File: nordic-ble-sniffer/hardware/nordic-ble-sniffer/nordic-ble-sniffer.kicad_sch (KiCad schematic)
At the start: 23 parts, among them J2 USB2UART, U1 nRF52833_QDxx, U2 USBLC6-2P6, Y1 32MHz

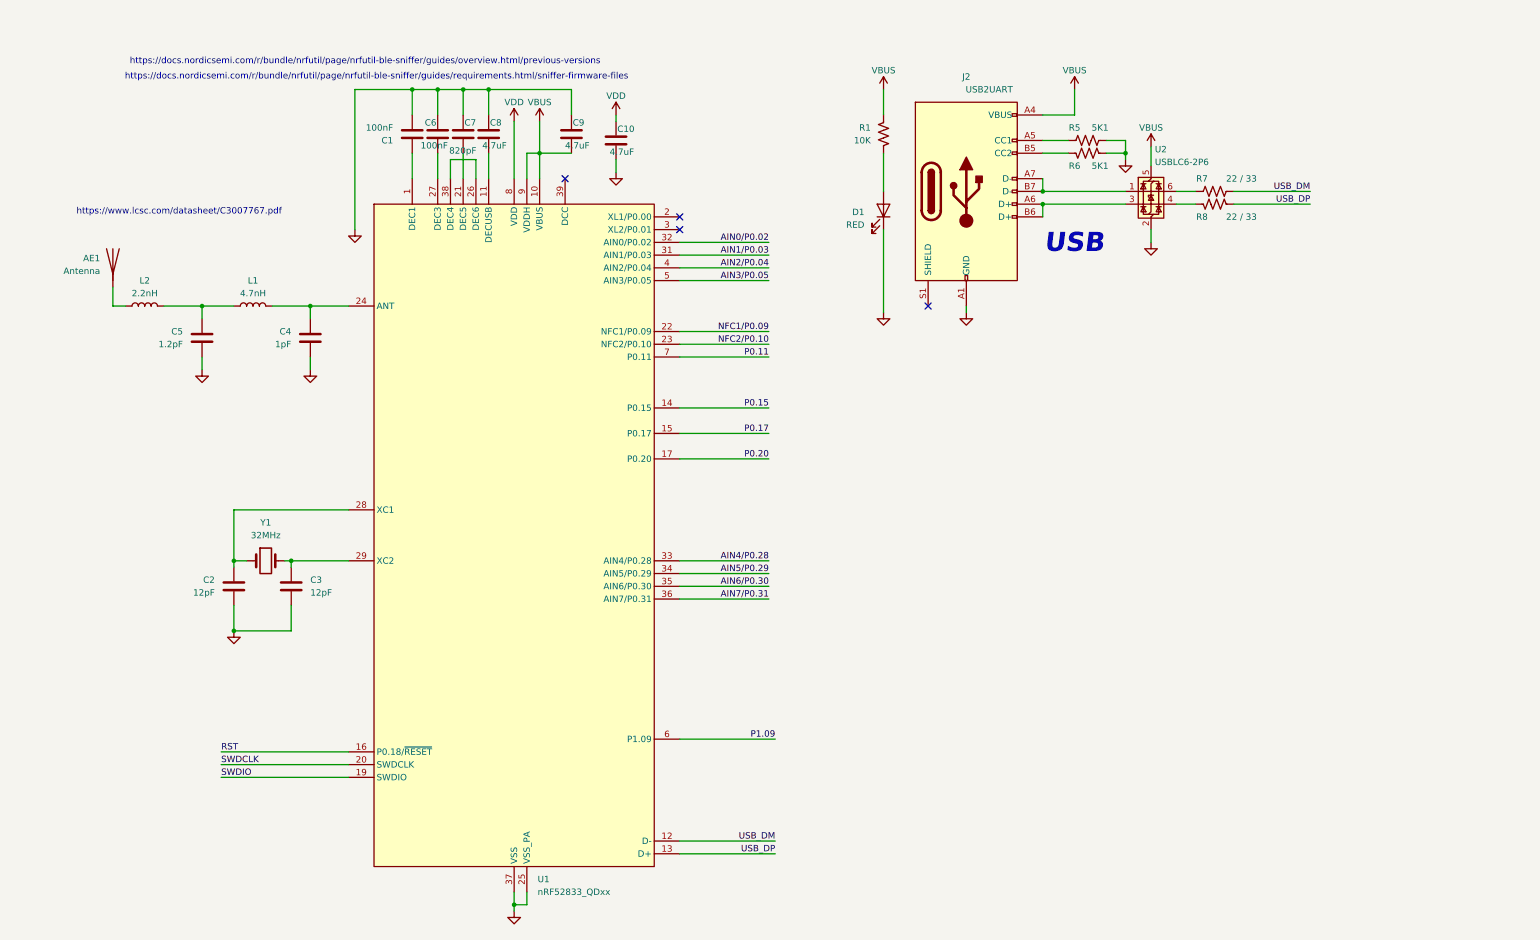
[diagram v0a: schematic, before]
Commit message: finish schematic ble sniffer with nrf52833 qfn40
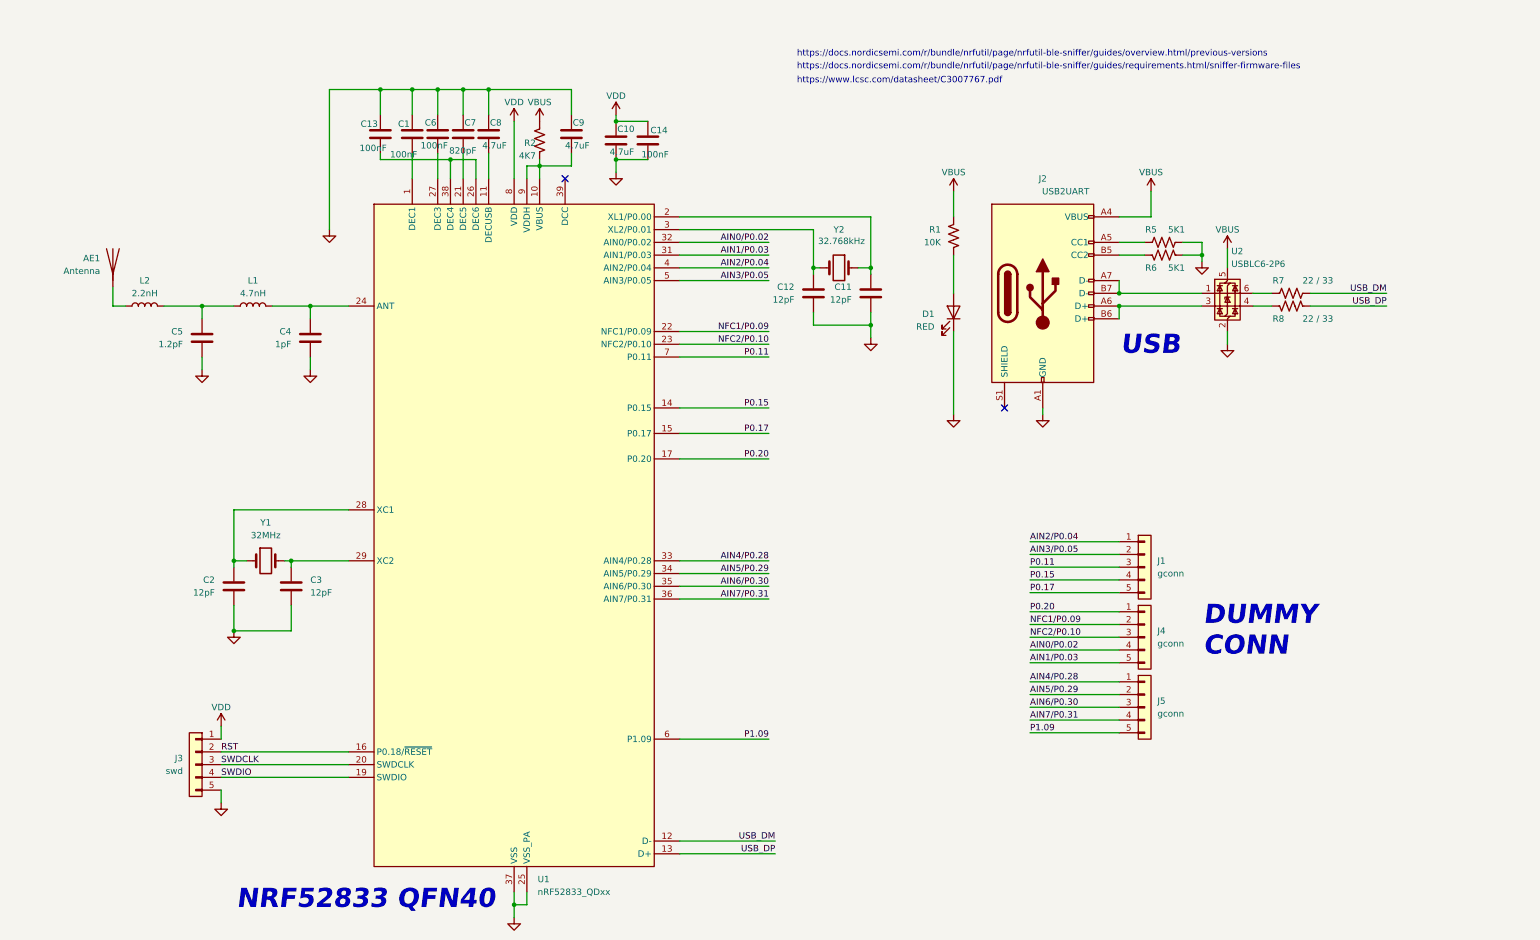
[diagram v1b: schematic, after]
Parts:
- added C11, C12: 12pF, Capacitor_SMD:C_0805_2012Metric_Pad1.18x1.45mm_HandSolder, symbol Device:C
- added C13, C14: 100nF, Capacitor_SMD:C_0805_2012Metric_Pad1.18x1.45mm_HandSolder, symbol Device:C
- added J1, J4, J5: gconn, Connector_PinHeader_2.54mm:PinHeader_1x05_P2.54mm_Vertical, symbol Connector_Generic:Conn_01x05
- added J3: swd, Connector_PinHeader_2.54mm:PinHeader_1x05_P2.54mm_Vertical, symbol Connector_Generic:Conn_01x05
- added R2: 4K7, Resistor_SMD:R_0805_2012Metric_Pad1.20x1.40mm_HandSolder, symbol Device:R_US
- added Y2: 32.768kHz, Crystal:Crystal_HC49-U_Vertical, symbol Device:Crystal
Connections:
- net AIN0/P0.02: now also J4.4 (Pin_4)
- net AIN1/P0.03: now also J4.5 (Pin_5)
- net AIN2/P0.04: now also J1.1 (Pin_1)
- net AIN3/P0.05: now also J1.2 (Pin_2)
- net AIN4/P0.28: now also J5.1 (Pin_1)
- net AIN5/P0.29: now also J5.2 (Pin_2)
- net AIN6/P0.30: now also J5.3 (Pin_3)
- net AIN7/P0.31: now also J5.4 (Pin_4)
- net GND: now also C11.2, C12.2, C13.2, C14.1, J3.5 (Pin_5)
- net NFC1/P0.09: now also J4.2 (Pin_2)
- net NFC2/P0.10: now also J4.3 (Pin_3)
- net P0.11: now also J1.3 (Pin_3)
- net P0.15: now also J1.4 (Pin_4)
- net P0.17: now also J1.5 (Pin_5)
- net P0.20: now also J4.1 (Pin_1)
- net P1.09: now also J5.5 (Pin_5)
- net RST: now also J3.2 (Pin_2)
- net SWDCLK: now also J3.3 (Pin_3)
- net SWDIO: now also J3.4 (Pin_4)
- net VBUS: now also R2.1; no longer C9.2, U1.10 (VBUS), U1.9 (VDDH)
- net VDD: now also C14.2, J3.1 (Pin_1)
- net at U1.2 (XL1/P0.00): now also C11.1, Y2.1
- net at U1.26 (DEC6), U1.38 (DEC4): now also C13.1
- net at U1.3 (XL2/P0.01): now also C12.1, Y2.2
- new net: C9.2, R2.2, U1.10 (VBUS), U1.9 (VDDH)
- no-connect marks 4 -> 2
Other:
- note added: "DUMMY CONN"
- note added: "NRF52833 QFN40"
- title: (none) -> NRF52833 QFN40 BLE Sniffer Dongle
- moved on the sheet: D1, J2, R1, R5, R6, R7, R8, U2

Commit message: finish ble-sniffer routing but excluding dummy pin header
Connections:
- net SWDCLK: now also J3.4 (Pin_4); no longer J3.3 (Pin_3)
- net SWDIO: now also J3.3 (Pin_3); no longer J3.4 (Pin_4)
- no-connect marks 2 -> 3
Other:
- note added: "DUMMY CONN (Excluded)"
- note removed: "DUMMY CONN"
